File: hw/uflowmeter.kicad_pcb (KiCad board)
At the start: 4 copper layers, 70 x 55 mm, 54 parts, among them J1 SBW, J2 ANT, J3 Display, J4 Transducers, J5 Cal UART, Q1 IRLML6401, SW1 Button, U1 MSP430FR5043IRGC, U2 CC1101RGPR, Y1 32.768kHz, Y2 8MHz, Y3 26MHz

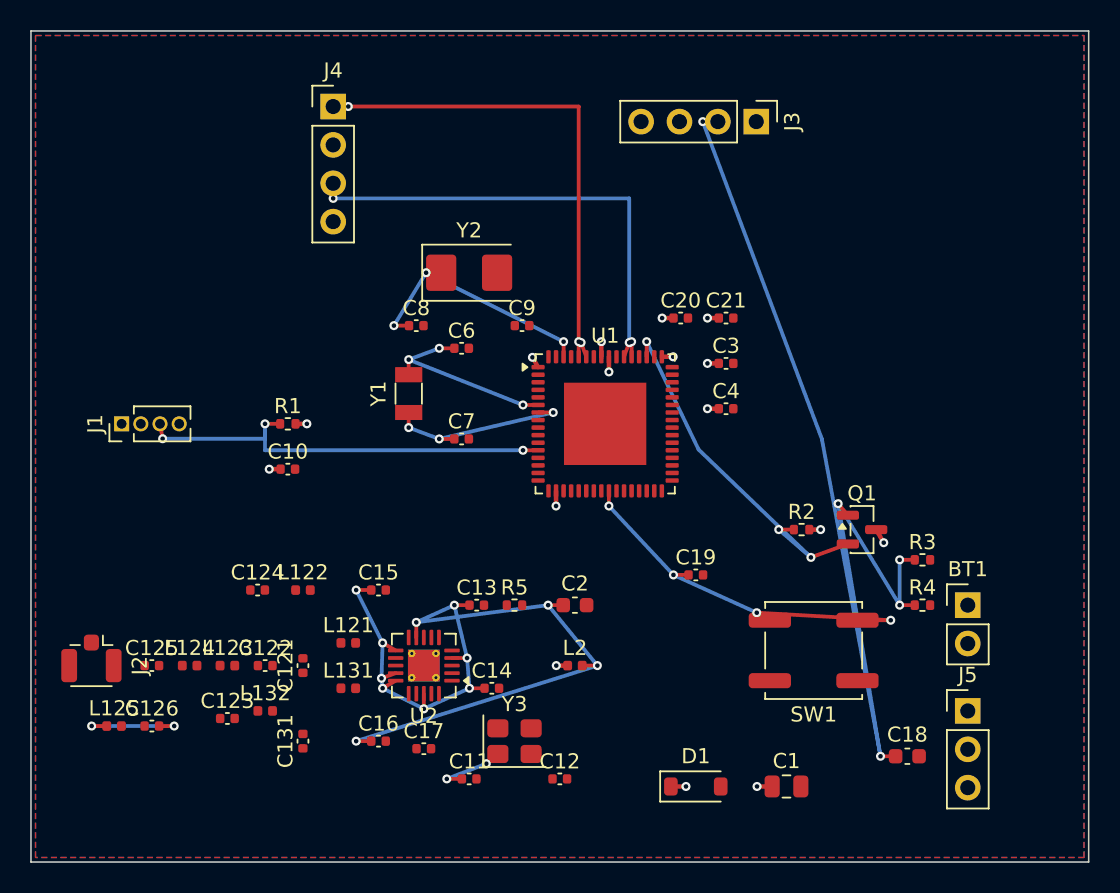
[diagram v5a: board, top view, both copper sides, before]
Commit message: hw: route with a grid router, so the tracks have a shape
route_maze.py is A* over a 0.1 mm grid on both layers, eight directions, a
via costed at about five millimetres of track. Octile movement is the point:
runs come out horizontal, vertical or at 45 degrees rather than as whatever
straight line happened to be clear, which is what the previous pass produced
and what looked wrong.

Three bugs, each of which cost a full run to find.

A cell claimed by two nets belongs to neither. On a 0.5 mm pitch package the
neighbouring pins' keep-outs overlap, and letting the first claimant own the
cell is how a track ends up crossing its neighbour's pad -- 67 violations
that way, the first time.

The keep-out cannot be generous. It is painted as a rectangle, so a margin
much over the 0.275 mm the rules actually need closes the one way out of a
QFN pin, which is straight outward along the pin's own axis. At 0.38 mm
nothing escaped at all and every net that touched the CC1101 failed.

And connectivity is per layer. Seeding the search from both layers of a
surface-mount pad let runs start on the side with no copper, so tracks were
laid that connected nothing -- 68 unconnected items while the router reported
seventeen nets done.

route_escape.py still runs afterwards to pick up what the grid router could
not reach. Its tracks are the long arbitrary diagonals and they are the ones
worth redoing by hand.

37 unconnected, down from 134 at placement. DRC clean. Both routers are kept
in hw/ so the board can be rebuilt from the netlist.

Co-Authored-By: Claude Opus 5 (1M context) <noreply@anthropic.com>
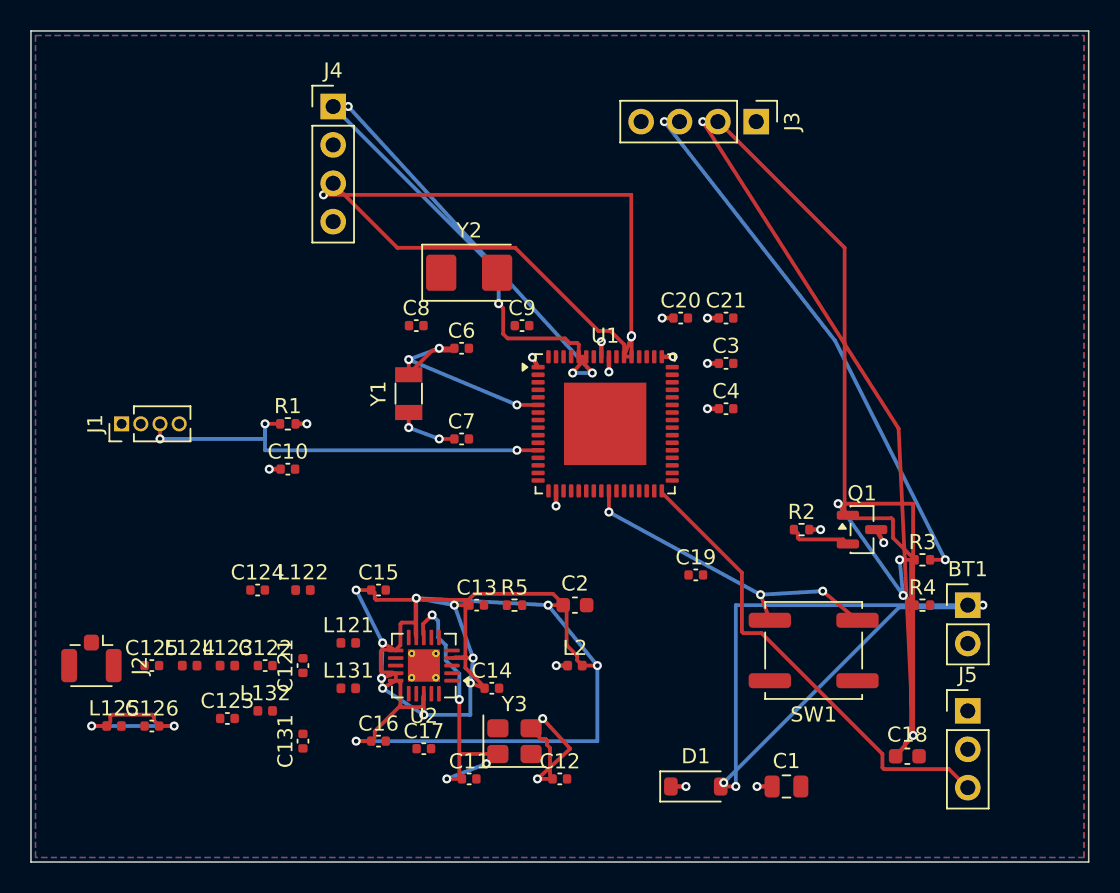
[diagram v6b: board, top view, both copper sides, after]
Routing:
- net VCC_DISP: track 76.6 -> 128.1 mm
- net BAT+: track 0.00 -> 51.1 mm, vias 0 -> 3
- net RADIO_VDD: track 64.3 -> 111.6 mm
- net I2C_SCL: track 0.00 -> 36.6 mm, vias 0 -> 2
- net UART_RX: track 0.00 -> 30.7 mm
- net CH1: track 32.3 -> 58.0 mm
- net DISP_GATE: track 25.6 -> 3.62 mm, vias 3 -> 0
- net CH0: track 34.0 -> 54.7 mm, vias 3 -> 4
- net USSXTIN: track 17.3 -> 0.00 mm, vias 3 -> 0
- net XOSC_Q1: track 4.80 -> 20.1 mm, vias 2 -> 4
- net XOSC_Q2: track 0.00 -> 11.2 mm, vias 0 -> 2
- net LFXOUT: track 12.9 -> 4.15 mm, vias 3 -> 2
- net BUTTON: track 26.4 -> 21.8 mm, vias 4 -> 3
- net RFNOTCH: track 7.47 -> 11.3 mm
- net LFXIN: track 13.3 -> 16.6 mm

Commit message: hw: escape a 0.5 mm pitch QFN with 0.15 mm track, not 0.25
At 0.25 mm nothing could leave U1 or U2 at all, and the grid map shows why.
The neighbouring pins sit 0.5 mm away and are 0.3 mm wide, so their copper
edge is 0.35 mm from a pin's own axis. A 0.25 mm track needs 0.275 mm of room
from its centreline; the two neighbours' keep-outs then meet over the escape
corridor and close it. There is a solid three-cell band under every pin that
belongs to two nets at once and so may be used by neither.

At 0.15 mm the track needs 0.225 mm, the keep-outs stop short of each other,
and the corridor opens. That is why fine-pitch escapes are routed thin and
widened once clear of the package, and the widening is worth doing by hand on
anything carrying current.

Finding it took printing the occupancy grid around one pin and looking at it,
after four rounds of guessing at clearances -- 0.38 mm let nothing out, 0.30
let nothing out either, 0.25 opened the corridor but left four real clearance
violations, and 0.29 with the thinner track is clean.

Default net class is now 0.15 mm to match. 37 unconnected, DRC clean.

Co-Authored-By: Claude Opus 5 (1M context) <noreply@anthropic.com>
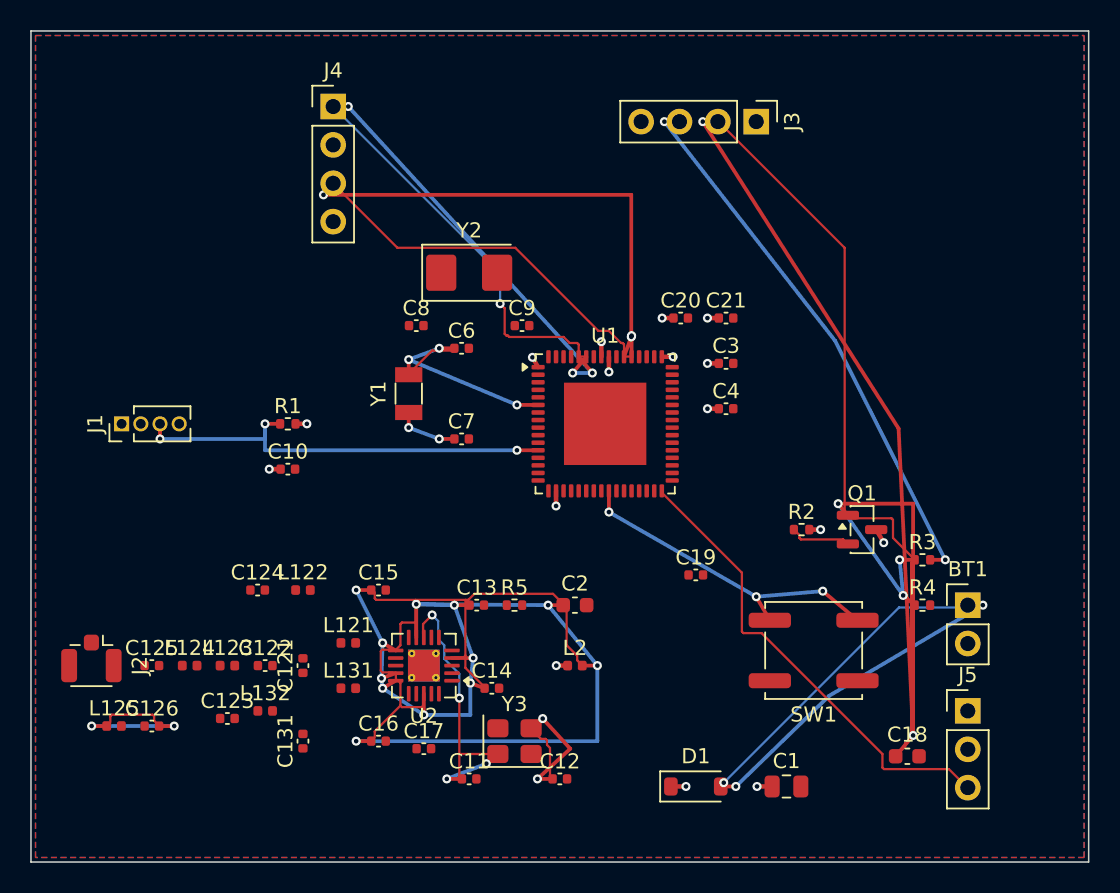
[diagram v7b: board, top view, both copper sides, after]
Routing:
- net BAT+: track 51.1 -> 43.1 mm

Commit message: hw: finer grid, no corner cutting, and a cleanup pass -- 34 unconnected
Three changes, in the order they mattered.

The grid went to 0.05 mm. At 0.1 mm the escape corridor beside a QFN pin is
narrower than one cell and simply vanishes, which is what had been capping
the result. Making it affordable needed a weighted heuristic and bounding
each search to the box its net lives in, together worth more than an order of
magnitude; a run is now two and a half minutes.

Diagonal steps no longer cut corners. A 45 degree move sweeps the two cells
beside it, and letting it clip one is how a track ends up a hair too close to
the pin next door.

route_cleanup.py drops whatever DRC still objects to. The routers model
clearance as inflated rectangles on a grid, close to KiCad's computation but
not identical, and where they disagree KiCad is right. Better to leave two
connections for a person than to ship a board that fails its own rule check.

Also tried and worth recording as a dead end: reordering the nets. Five
orderings scored 23 to 26 connections, and the one already in use was joint
best, so the order was never the lever.

34 unconnected, of which seventeen are the RF chain left alone on purpose.
355 tracks, 60 vias, DRC clean.

Co-Authored-By: Claude Opus 5 (1M context) <noreply@anthropic.com>
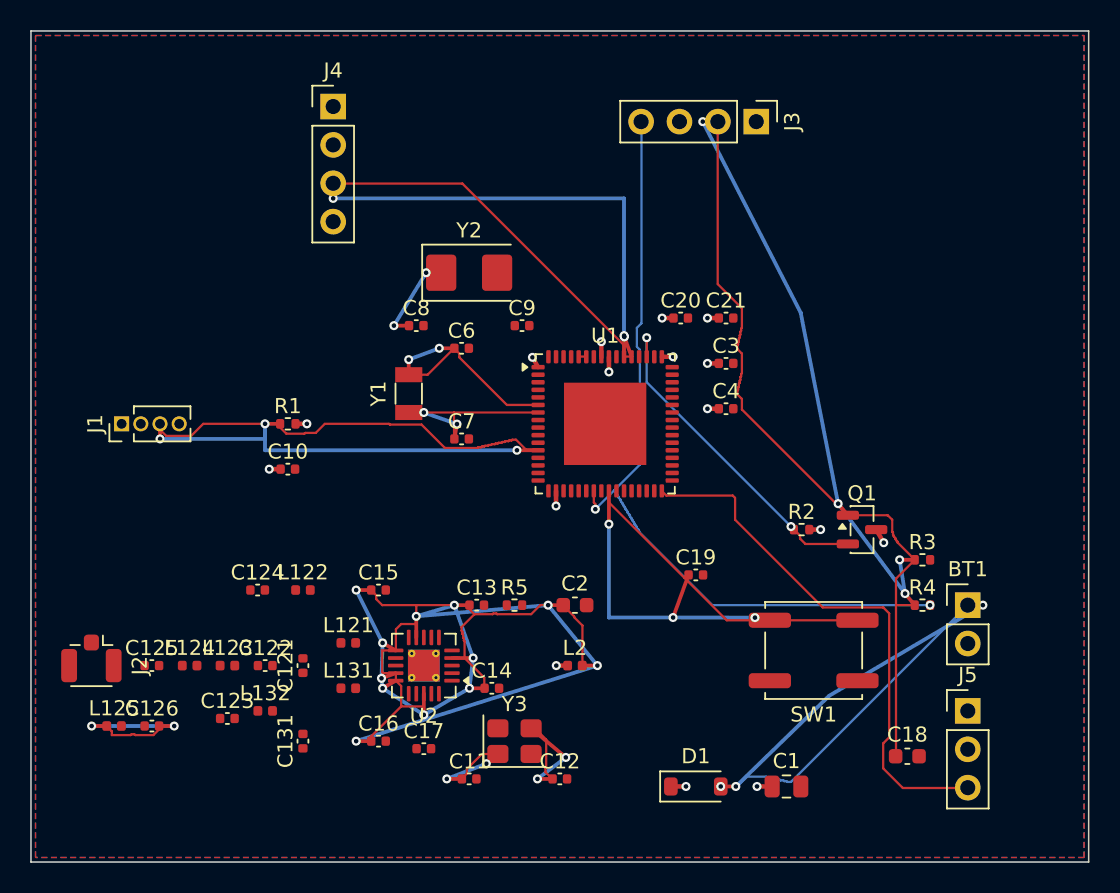
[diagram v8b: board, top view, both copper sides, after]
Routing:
- net CH0: track 54.6 -> 0.30 mm, vias 4 -> 0
- net I2C_SDA: track 0.00 -> 52.8 mm, vias 0 -> 2
- net VCC_DISP: track 128.1 -> 91.2 mm, vias 5 -> 4
- net I2C_SCL: track 36.6 -> 0.00 mm, vias 2 -> 0
- net RST: track 29.8 -> 56.8 mm
- net BUTTON: track 21.9 -> 42.3 mm
- net DISP_GATE: track 3.57 -> 21.6 mm, vias 0 -> 2
- net XOSC_Q1: track 20.1 -> 7.82 mm, vias 4 -> 2
- net LFXOUT: track 4.15 -> 14.3 mm
- net USSXTIN: track 0.00 -> 6.10 mm, vias 0 -> 2
- net RADIO_VDD: track 111.2 -> 105.5 mm
- net UART_RX: track 30.7 -> 35.6 mm
- net LFXIN: track 16.6 -> 14.6 mm, vias 3 -> 2
- net CH1: track 58.0 -> 56.7 mm
- net XOSC_Q2: track 11.2 -> 10.2 mm
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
